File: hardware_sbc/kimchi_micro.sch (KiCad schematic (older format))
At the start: 35 parts, among them J1 Conn_01x06, J2 Conn_01x06, J3 Conn_01x04_MountingPin, J4 Conn_02x05_Odd_Even, SW1 SW_Push, SW2 SW_Push, SW3 SW_Push, U1 IMX8MM, U2 24C32, Y1 Crystal_GND24

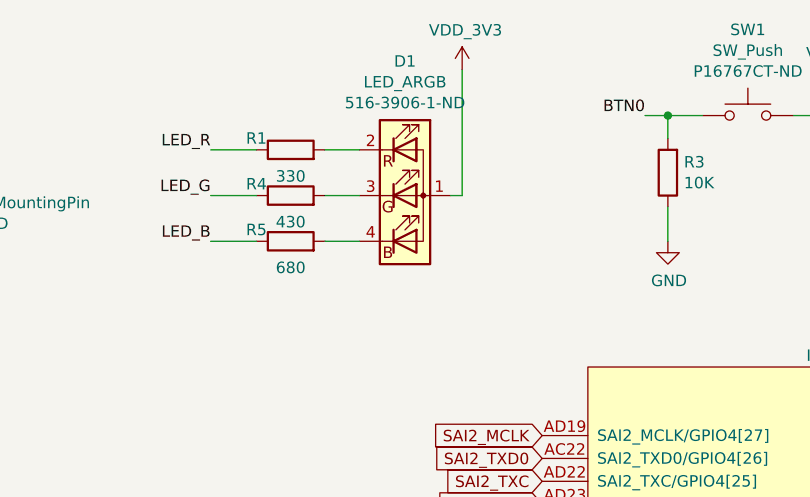
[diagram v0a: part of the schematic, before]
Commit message: Replace system and charger LEDs with smaller 0404 RGB LED
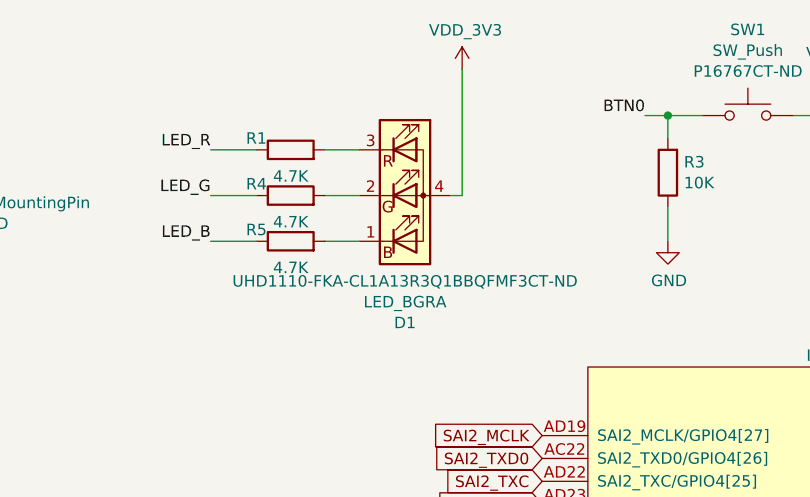
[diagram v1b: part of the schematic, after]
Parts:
- removed D1: LED_ARGB, LED_SMD:LED_Cree-PLCC4_2x2mm_CW, symbol Device:LED_ARGB
- added D1: LED_BGRA, mxenc:LED_0404, symbol Device:LED_BGRA
- R1: value 330 -> 4.7K; Mfgrpart RC0201JR-07330RL -> RC0201JR-074K7L; Vendorpart 311-330NCT-ND -> 311-4.7KNCT-ND
- R4: value 430 -> 4.7K; Mfgrpart RC0201JR-07430RL -> RC0201JR-074K7L; Vendorpart YAG2900CT-ND -> 311-4.7KNCT-ND
- R5: value 680 -> 4.7K; Mfgrpart RC0201JR-07680RL -> RC0201JR-074K7L; Vendorpart 311-680NCT-ND -> 311-4.7KNCT-ND
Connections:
- net VDD_3V3: now also D1.4 (A)
- net at R1.2: now also D1.3 (RK)
- net at R4.2: now also D1.2 (GK)
- net at R5.2: now also D1.1 (BK)
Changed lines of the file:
@@
 BTN0
-$Comp
-L Device:LED_ARGB D1
-U 1 1 5D8BE79A
-P 7300 1500
-F 0 "D1" H 7300 2087 50  0000 C CNN
-F 1 "LED_ARGB" H 7300 1996 50  0000 C CNN
-F 2 "LED_SMD:LED_Cree-PLCC4_2x2mm_CW" H 7300 1450 50  0001 C CNN
-F 3 "~" H 7300 1450 50  0001 C CNN
-F 4 "516-3906-1-ND" H 7300 1905 50  0000 C CNN "Vendorpart"
-F 5 "Broadcom" H 7300 1500 50  0001 C CNN "Mfgr"
-F 6 "" H 7300 1500 50  0001 C CNN "Part"
-F 7 "ASMB-KTF0-0A306" H 7300 1500 50  0001 C CNN "Mfgrpart"
-	1    7300 1500
-	1    0    0    -1
-$EndComp
 $Comp
 L mxenc:MIMX8MM6DVTLZAA U1
@@
 Wire Wire Line
 	7550 1500 7500 1500
-$Comp
-L Device:R R1
-U 1 1 5DA0DC86
-P 6800 1300
-F 0 "R1" V 6850 1450 50  0000 C CNN
-F 1 "330" V 6684 1300 50  0000 C CNN
-F 2 "Resistor_SMD:R_0201_0603Metric" V 6730 1300 50  0001 C CNN
-F 3 "~" H 6800 1300 50  0001 C CNN
-F 4 "Yageo" H 6800 1300 50  0001 C CNN "Mfgr"
-F 5 "" H 6800 1300 50  0001 C CNN "Part"
-F 6 "311-330NCT-ND" H 6800 1300 50  0001 C CNN "Vendorpart"
-F 7 "RC0201JR-07330RL" H 6800 1300 50  0001 C CNN "Mfgrpart"
-	1    6800 1300
-	0    -1   -1   0
-$EndComp
-$Comp
-L Device:R R4
-U 1 1 5DA267EA
-P 6800 1500
-F 0 "R4" V 6850 1650 50  0000 C CNN
-F 1 "430" V 6684 1500 50  0000 C CNN
-F 2 "Resistor_SMD:R_0201_0603Metric" V 6730 1500 50  0001 C CNN
-F 3 "~" H 6800 1500 50  0001 C CNN
-F 4 "Yageo" H 6800 1500 50  0001 C CNN "Mfgr"
-F 5 "" H 6800 1500 50  0001 C CNN "Part"
-F 6 "YAG2900CT-ND" H 6800 1500 50  0001 C CNN "Vendorpart"
-F 7 "RC0201JR-07430RL" H 6800 1500 50  0001 C CNN "Mfgrpart"
-	1    6800 1500
-	0    -1   -1   0
-$EndComp
-$Comp
-L Device:R R5
-U 1 1 5DA26C62
-P 6800 1700
-F 0 "R5" V 6850 1850 50  0000 C CNN
-F 1 "680" V 6684 1700 50  0000 C CNN
-F 2 "Resistor_SMD:R_0201_0603Metric" V 6730 1700 50  0001 C CNN
-F 3 "~" H 6800 1700 50  0001 C CNN
-F 4 "Yageo" H 6800 1700 50  0001 C CNN "Mfgr"
-F 5 "" H 6800 1700 50  0001 C CNN "Part"
-F 6 "311-680NCT-ND" H 6800 1700 50  0001 C CNN "Vendorpart"
-F 7 "RC0201JR-07680RL" H 6800 1700 50  0001 C CNN "Mfgrpart"
-	1    6800 1700
-	0    -1   -1   0
-$EndComp
 Wire Wire Line
 	6950 1300 7100 1300
@@
 	7700 5350 7900 5350
 NoConn ~ 5600 3550
+$Comp
+L Device:LED_BGRA D?
+U 1 1 603828EF
+P 7300 1500
+AR Path="/5DC6F4F1/603828EF" Ref="D?"  Part="1"
+AR Path="/603828EF" Ref="D1"  Part="1"
+F 0 "D1" H 7300 943 50  0000 C CNN
+F 1 "LED_BGRA" H 7300 1034 50  0000 C CNN
+F 2 "mxenc:LED_0404" H 7300 1450 50  0001 C CNN
+F 3 "~" H 7300 1450 50  0001 C CNN
+F 4 "UHD1110-FKA-CL1A13R3Q1BBQFMF3CT-ND " H 7300 1125 50  0000 C CNN "Vendorpart"
+F 5 "Cree" H 7300 1500 50  0001 C CNN "Mfgr"
+F 6 "UHD1110-FKA" H 7300 1500 50  0001 C CNN "Mfgrpart"
+	1    7300 1500
+	1    0    0    -1
+$EndComp
+$Comp
+L Device:R R1
+U 1 1 603DF8EB
+P 6800 1300
+AR Path="/603DF8EB" Ref="R1"  Part="1"
+AR Path="/5DC6F4F1/603DF8EB" Ref="R?"  Part="1"
+F 0 "R1" V 6850 1450 50  0000 C CNN
+F 1 "4.7K" V 6684 1300 50  0000 C CNN
+F 2 "Resistor_SMD:R_0201_0603Metric" V 6730 1300 50  0001 C CNN
+F 3 "~" H 6800 1300 50  0001 C CNN
+F 4 "Yageo" H 6800 1300 50  0001 C CNN "Mfgr"
+F 5 "" H 6800 1300 50  0001 C CNN "Part"
+F 6 "311-4.7KNCT-ND" H 6800 1300 50  0001 C CNN "Vendorpart"
+F 7 "RC0201JR-074K7L" H 6800 1300 50  0001 C CNN "Mfgrpart"
+	1    6800 1300
+	0    -1   -1   0
+$EndComp
+$Comp
+L Device:R R4
+U 1 1 603EAC16
+P 6800 1500
+AR Path="/603EAC16" Ref="R4"  Part="1"
+AR Path="/5DC6F4F1/603EAC16" Ref="R?"  Part="1"
+F 0 "R4" V 6850 1650 50  0000 C CNN
+F 1 "4.7K" V 6684 1500 50  0000 C CNN
+F 2 "Resistor_SMD:R_0201_0603Metric" V 6730 1500 50  0001 C CNN
+F 3 "~" H 6800 1500 50  0001 C CNN
+F 4 "Yageo" H 6800 1500 50  0001 C CNN "Mfgr"
+F 5 "" H 6800 1500 50  0001 C CNN "Part"
+F 6 "311-4.7KNCT-ND" H 6800 1500 50  0001 C CNN "Vendorpart"
+F 7 "RC0201JR-074K7L" H 6800 1500 50  0001 C CNN "Mfgrpart"
+	1    6800 1500
+	0    -1   -1   0
+$EndComp
+$Comp
+L Device:R R5
+U 1 1 603F5DA7
+P 6800 1700
+AR Path="/603F5DA7" Ref="R5"  Part="1"
+AR Path="/5DC6F4F1/603F5DA7" Ref="R?"  Part="1"
+F 0 "R5" V 6850 1850 50  0000 C CNN
+F 1 "4.7K" V 6684 1700 50  0000 C CNN
+F 2 "Resistor_SMD:R_0201_0603Metric" V 6730 1700 50  0001 C CNN
+F 3 "~" H 6800 1700 50  0001 C CNN
+F 4 "Yageo" H 6800 1700 50  0001 C CNN "Mfgr"
+F 5 "" H 6800 1700 50  0001 C CNN "Part"
+F 6 "311-4.7KNCT-ND" H 6800 1700 50  0001 C CNN "Vendorpart"
+F 7 "RC0201JR-074K7L" H 6800 1700 50  0001 C CNN "Mfgrpart"
+	1    6800 1700
+	0    -1   -1   0
+$EndComp
 $EndSCHEMATC
